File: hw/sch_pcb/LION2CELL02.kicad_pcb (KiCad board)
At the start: 2 copper layers, 80.8 x 60.5 mm, 104 parts, among them J1 USBC_USB4105-GF-A, J10 HEADER_2x01_PARALLEL, J11 HEADER_1x02, J12 HEADER_2x05_PARALLEL, J2 CONN1_1, J3 CONN1_1, J4 JUMP_4X2, J5 HEADER_2x03_PARALLEL, J6 HEADER_2x01_PARALLEL, J7 HEADER_2x01_PARALLEL, J8 CONN1_1, J9 CONN1_1, Q1 DMTH3002LPS, Q2 AP2305AGN-HF-3, Q3 DMTH3002LPS, Q5 DMTH3002LPS, SW1 SW_Push, SW2 SW_Push, U1 BQ25792RQMR1, U2 LMR14050, U3 BQ40z50-R2

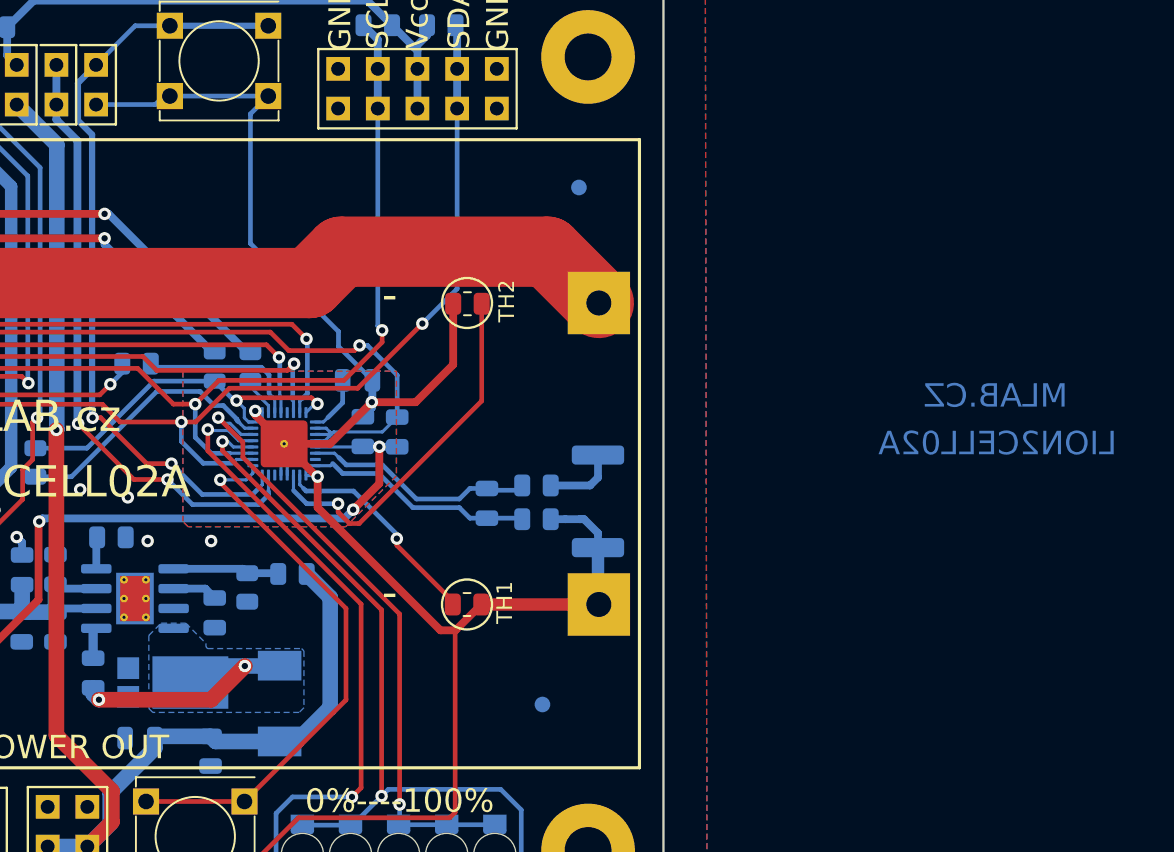
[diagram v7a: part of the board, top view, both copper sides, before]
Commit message: Resolve DRC issues. Update footprints. Improve silkscreen.
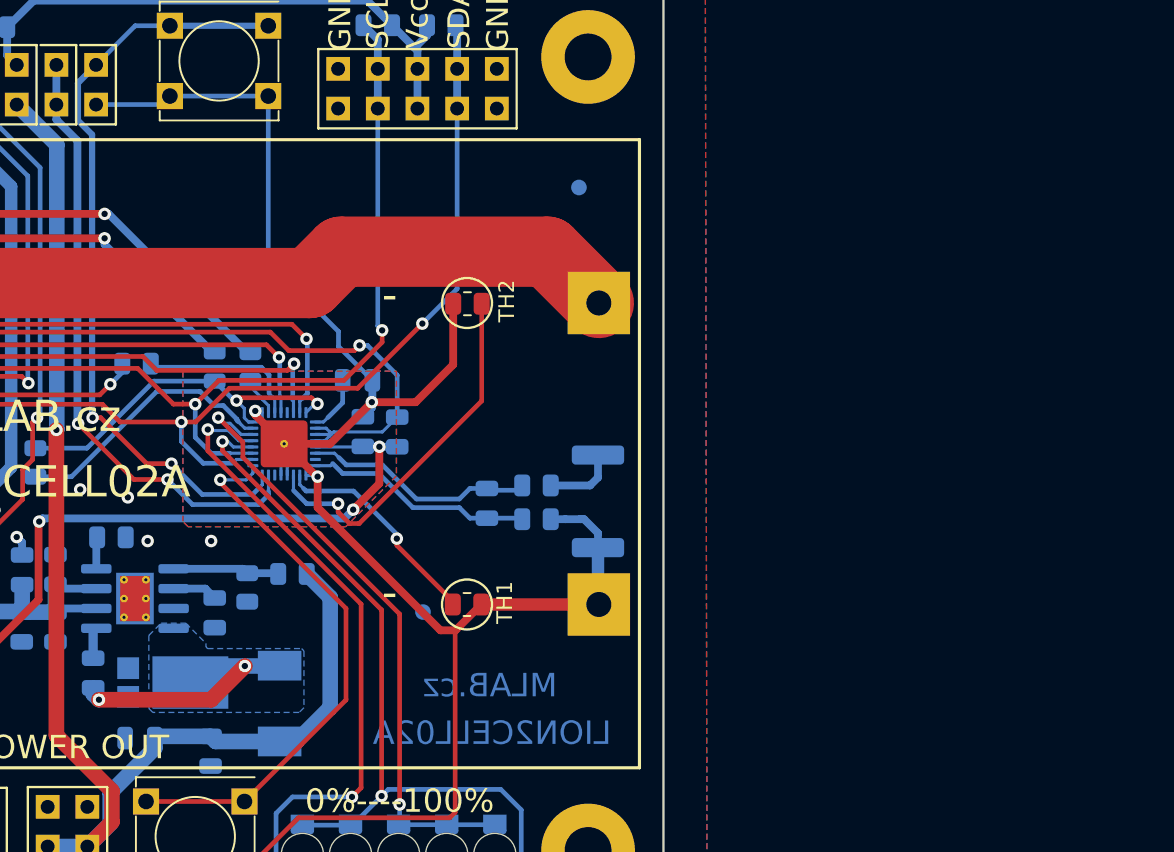
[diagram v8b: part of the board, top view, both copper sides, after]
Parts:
- moved FID3 9.67 mm to (173.5, 115.1)
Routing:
- net GND1: track 131.6 -> 130.9 mm
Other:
- board text removed: "MLAB.CZ"
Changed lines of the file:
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@@
 			)
 		)
+		(property "UST_ID" ""
+			(at 0 0 90)
+			(unlocked yes)
+			(layer "F.Fab")
+			(hide yes)
+			(effects
+				(font
+					(size 1 1)
+					(thickness 0.15)
+				)
+			)
+		)
 		(sheetname "Power Output")
 		(sheetfile "power_output.kicad_sch")
@@
 		(tags "resistor")
 		(property "Reference" "R4"
-			(at 0 1.65 0)
+			(at -0.9906 1.7526 0)
 			(layer "B.SilkS")
 			(effects
@@
 		(sheetname "Root")
 		(sheetfile "LION2CELL02.kicad_sch")
-		(attr smd)
+		(attr smd exclude_from_bom)
 		(fp_circle
 			(center 0 0)
@@
 		(sheetname "Root")
 		(sheetfile "LION2CELL02.kicad_sch")
-		(attr smd)
+		(attr smd exclude_from_bom)
 		(fp_circle
 			(center 0 0)
@@
 		(sheetname "Root")
 		(sheetfile "LION2CELL02.kicad_sch")
-		(attr smd)
+		(attr smd exclude_from_bom)
 		(fp_circle
 			(center 0 0)
@@
 	(footprint "Fiducial:Fiducial_1mm_Mask2mm"
 		(layer "B.Cu")
-		(at 181.139 121.0528 180)
+		(at 173.4936 115.1346 180)
 		(descr "Circular Fiducial, 1mm bare copper, 2mm soldermask opening (Level A)")
 		(tags "fiducial")
@@
 		(sheetname "Root")
 		(sheetfile "LION2CELL02.kicad_sch")
-		(attr smd)
+		(attr smd exclude_from_bom)
 		(fp_circle
 			(center 0 0)
@@
 		(layer "Edge.Cuts")
 	)
-	(gr_text "MLAB.CZ"
-		(at 210.1458 101.2916 0)
-		(layer "B.Cu")
+	(gr_text "MLAB.cz"
+		(at 177.7862 119.8336 0)
+		(layer "B.Cu" knockout)
 		(effects
 			(font
@@
 	)
 	(gr_text "LION2CELL02A"
-		(at 210.2728 104.3396 0)
-		(layer "B.Cu")
+		(at 177.9132 122.8816 0)
+		(layer "B.Cu" knockout)
 		(effects
 			(font
@@
 	)
 	(segment
+		(start 163.5876 92.681)
+		(end 168.0834 97.1768)
+		(width 0.3)
+		(layer "B.Cu")
+		(net 3)
+	)
+	(segment
 		(start 184.695 110.08)
 		(end 184.695 111.01)
@@
 	)
 	(segment
+		(start 156.8926 82.4994)
+		(end 156.744 82.648)
+		(width 0.3)
+		(layer "B.Cu")
+		(net 3)
+	)
+	(segment
 		(start 163.202104 102.366496)
 		(end 162.859703 102.366496)
@@
 	)
 	(segment
-		(start 156.8926 82.104)
-		(end 156.3486 82.648)
+		(start 168.0834 98.134792)
+		(end 170.251104 100.302496)
 		(width 0.3)
 		(layer "B.Cu")
@@
 	)
 	(segment
+		(start 163.5876 82.1044)
+		(end 163.5876 92.681)
+		(width 0.3)
+		(layer "B.Cu")
+		(net 3)
+	)
+	(segment
+		(start 156.744 82.648)
+		(end 152.564 82.648)
+		(width 0.3)
+		(layer "B.Cu")
+		(net 3)
+	)
+	(segment
 		(start 182.611 109.191)
 		(end 183.552 109.191)
@@
 	)
 	(segment
+		(start 168.0834 97.1768)
+		(end 168.0834 98.134792)
+		(width 0.3)
+		(layer "B.Cu")
+		(net 3)
+	)
+	(segment
 		(start 157.288 82.104)
 		(end 163.588 82.104)
@@
 	)
 	(segment
-		(start 168.0834 98.134792)
-		(end 170.251104 100.302496)
+		(start 156.8926 82.104)
+		(end 156.8926 82.4994)
 		(width 0.3)
 		(layer "B.Cu")
@@
 	)
 	(segment
-		(start 163.588 82.104)
-		(end 162.445 83.247)
-		(width 0.3)
-		(layer "B.Cu")
-		(net 3)
-	)
-	(segment
 		(start 183.552 109.191)
 		(end 183.679 109.318)
@@
 	)
 	(segment
-		(start 162.445 83.247)
-		(end 162.445 91.5384)
-		(width 0.3)
-		(layer "B.Cu")
-		(net 3)
-	)
-	(segment
 		(start 164.802104 106.366496)
 		(end 164.802104 104.566496)
@@
 	)
 	(segment
-		(start 162.445 91.5384)
-		(end 168.0834 97.1768)
-		(width 0.3)
-		(layer "B.Cu")
-		(net 3)
-	)
-	(segment
-		(start 156.3486 82.648)
-		(end 152.564 82.648)
-		(width 0.3)
-		(layer "B.Cu")
-		(net 3)
-	)
-	(segment
-		(start 168.0834 97.1768)
-		(end 168.0834 98.134792)
+		(start 163.588 82.104)
+		(end 163.5876 82.1044)
 		(width 0.3)
 		(layer "B.Cu")
@@
 	)
 	(zone
-		(net 39)
-		(net_name "Net-(Q5-G)")
+		(net 12)
+		(net_name "/Fuel Gauge/PACK+")
 		(layer "B.Cu")
-		(name "$teardrop_padvia$")
-		(hatch full 0.1)
-		(priority 30001)
-		(attr
-			(teardrop
-				(type padvia)
-			)
-		)
+		(hatch edge 0.5)
+		(priority 3)
 		(connect_pads yes
-			(clearance 0)
+			(clearance 0.5)
 		)
-		(min_thickness 0.0254)
+		(min_thickness 0.25)
 		(filled_areas_thickness no)
 		(fill yes
 			(thermal_gap 0.5)
 			(thermal_bridge_width 0.5)
-			(island_removal_mode 1)
-			(island_area_min 10)
 		)
 		(polygon
 			(pts
-				(xy 135.473 90.545) (xy 135.473 90.245) (xy 135.168 90.09) (xy 134.532 90.395) (xy 135.168 90.7)
+				(xy 133.514 85.188) (xy 136.9176 85.188) (xy 138.6956 86.966) (xy 138.6956 87.1692) (xy 138.7464 87.22)
+				(xy 144.3598 87.22) (xy 144.69 87.5502) (xy 144.69 92.7318) (xy 133.6664 92.7318) (xy 133.514 92.5794)
 			)
 		)
 	)
 	(zone
-		(net 12)
-		(net_name "/Fuel Gauge/PACK+")
+		(net 34)
+		(net_name "Net-(Q1-G)")
 		(layer "B.Cu")
-		(hatch edge 0.5)
-		(priority 3)
+		(name "$teardrop_padvia$")
+		(hatch full 0.1)
+		(priority 30002)
+		(attr
+			(teardrop
+				(type padvia)
+			)
+		)
 		(connect_pads yes
-			(clearance 0.5)
+			(clearance 0)
 		)
-		(min_thickness 0.25)
+		(min_thickness 0.0254)
 		(filled_areas_thickness no)
 		(fill yes
 			(thermal_gap 0.5)
 			(thermal_bridge_width 0.5)
+			(island_removal_mode 1)
+			(island_area_min 10)
 		)
 		(polygon
 			(pts
-				(xy 133.514 85.188) (xy 136.9176 85.188) (xy 138.6956 86.966) (xy 138.6956 87.1692) (xy 138.7464 87.22)
-				(xy 144.3598 87.22) (xy 144.69 87.5502) (xy 144.69 92.7318) (xy 133.6664 92.7318) (xy 133.514 92.5794)
+				(xy 143.54147 86.1836) (xy 143.753601 85.971469) (xy 143.344 85.770413) (xy 143.038293 86.073293)
+				(xy 143.344 86.380429)
 			)
 		)
 	)
 	(zone
-		(net 11)
-		(net_name "/Power Input/Power_load")
+		(net 38)
+		(net_name "Net-(Q3-G)")
 		(layer "B.Cu")
-		(hatch edge 0.5)
-		(priority 4)
+		(name "$teardrop_padvia$")
+		(hatch full 0.1)
+		(priority 30000)
+		(attr
+			(teardrop
+				(type padvia)
+			)
+		)
 		(connect_pads yes
-			(clearance 0.5)
+			(clearance 0)
 		)
-		(min_thickness 0.25)
+		(min_thickness 0.0254)
 		(filled_areas_thickness no)
 		(fill yes
 			(thermal_gap 0.5)
 			(thermal_bridge_width 0.5)
+			(island_removal_mode 1)
+			(island_area_min 10)
 		)
 		(polygon
 			(pts
-				(xy 127.0878 80.3366) (xy 137.2224 80.3366) (xy 142.9628 86.077) (xy 142.9628 87.2708) (xy 139.0258 87.2708)
-				(xy 136.689 84.934) (xy 127.0878 84.934)
+				(xy 120.887 86.435) (xy 120.887 86.735) (xy 121.192 86.89) (xy 121.828 86.585) (xy 121.192 86.28)
 			)
 		)
 	)
 	(zone
-		(net 34)
-		(net_name "Net-(Q1-G)")
+		(net 39)
+		(net_name "Net-(Q5-G)")
 		(layer "B.Cu")
 		(name "$teardrop_padvia$")
 		(hatch full 0.1)
-		(priority 30002)
+		(priority 30001)
 		(attr
 			(teardrop
@@
 		(polygon
 			(pts
-				(xy 143.54147 86.1836) (xy 143.753601 85.971469) (xy 143.344 85.770413) (xy 143.038293 86.073293)
-				(xy 143.344 86.380429)
+				(xy 135.473 90.545) (xy 135.473 90.245) (xy 135.168 90.09) (xy 134.532 90.395) (xy 135.168 90.7)
+			)
+		)
+	)
+	(zone
+		(net 11)
+		(net_name "/Power Input/Power_load")
+		(layer "B.Cu")
+		(hatch edge 0.5)
+		(priority 4)
+		(connect_pads yes
+			(clearance 0.5)
+		)
+		(min_thickness 0.25)
+		(filled_areas_thickness no)
+		(fill yes
+			(thermal_gap 0.5)
+			(thermal_bridge_width 0.5)
+		)
+		(polygon
+			(pts
+				(xy 127.0878 80.3366) (xy 137.2224 80.3366) (xy 142.9628 86.077) (xy 142.9628 87.2708) (xy 139.0258 87.2708)
+				(xy 136.689 84.934) (xy 127.0878 84.934)
 			)
 		)
@@
 		)
 	)
-	(zone
-		(net 38)
-		(net_name "Net-(Q3-G)")
-		(layer "B.Cu")
-		(name "$teardrop_padvia$")
-		(hatch full 0.1)
-		(priority 30000)
-		(attr
-			(teardrop
-				(type padvia)
-			)
-		)
-		(connect_pads yes
-			(clearance 0)
-		)
-		(min_thickness 0.0254)
-		(filled_areas_thickness no)
-		(fill yes
-			(thermal_gap 0.5)
-			(thermal_bridge_width 0.5)
-			(island_removal_mode 1)
-			(island_area_min 10)
-		)
-		(polygon
-			(pts
-				(xy 120.887 86.435) (xy 120.887 86.735) (xy 121.192 86.89) (xy 121.828 86.585) (xy 121.192 86.28)
-			)
-		)
-	)
-	(group ""
-		(members "26be241b-a000-4ff2-9a1d-39646a201b71" "6f9a7937-e8ef-479d-8100-ee901e28e7bf")
-	)
 )
